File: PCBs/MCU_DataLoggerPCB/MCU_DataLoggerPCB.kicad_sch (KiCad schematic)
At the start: 25 parts, among them U1 24LC1025, U2 24LC1025, U3 DS1337S+, U4 ATMEGA328P-AU, Y1 32.768 kHz, Y2 16 MHz

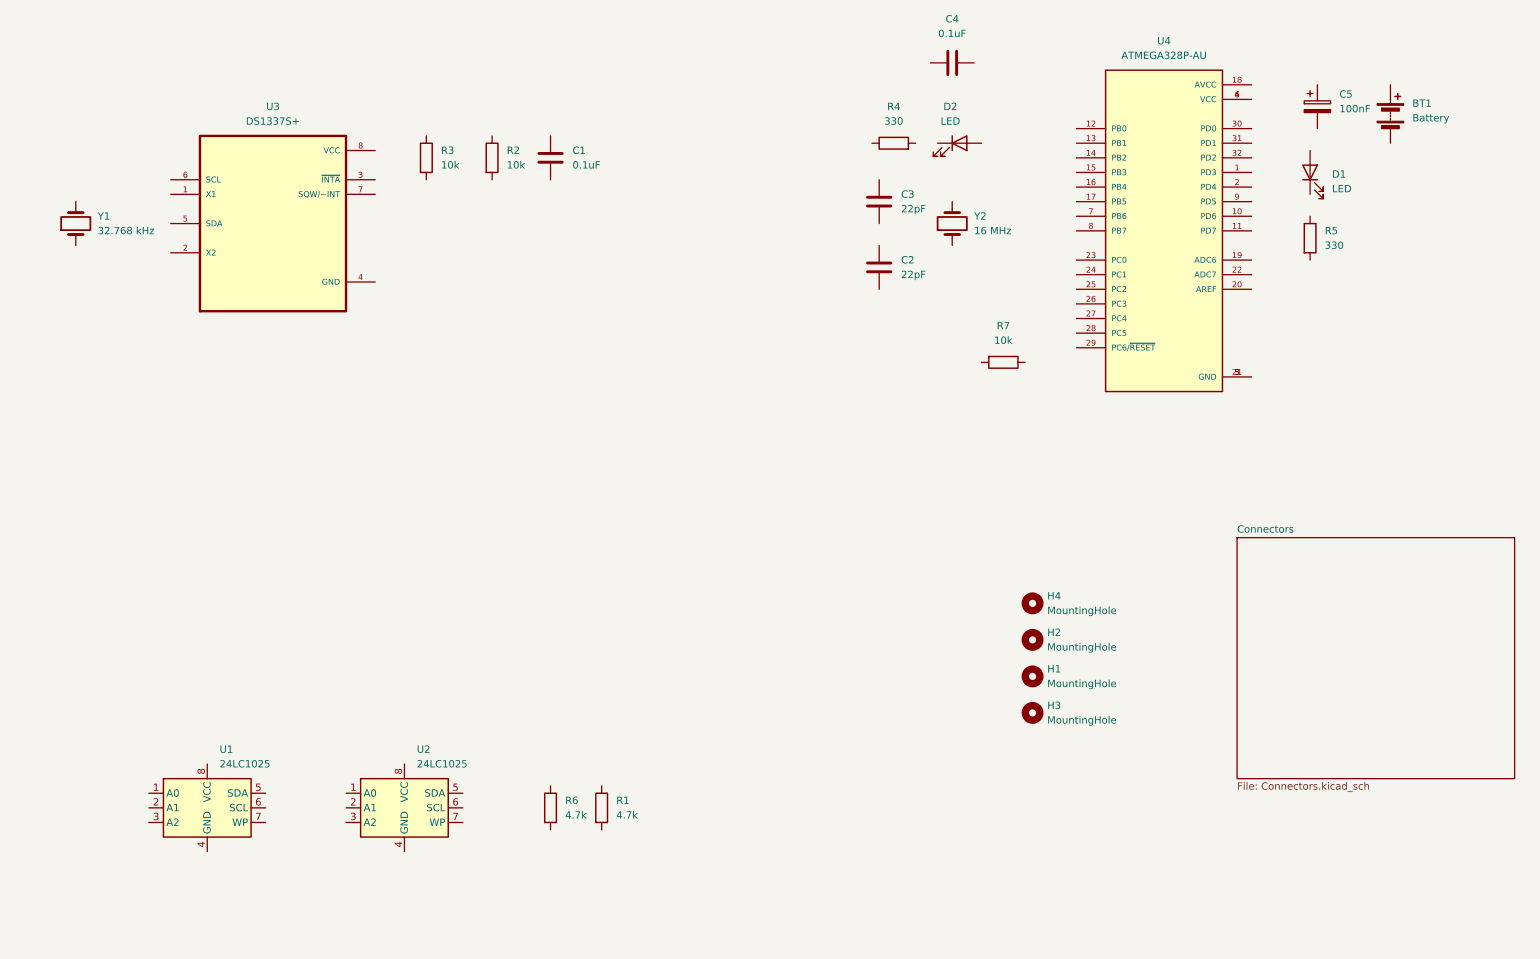
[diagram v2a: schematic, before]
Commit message: Project: completed wiring of the main sheet
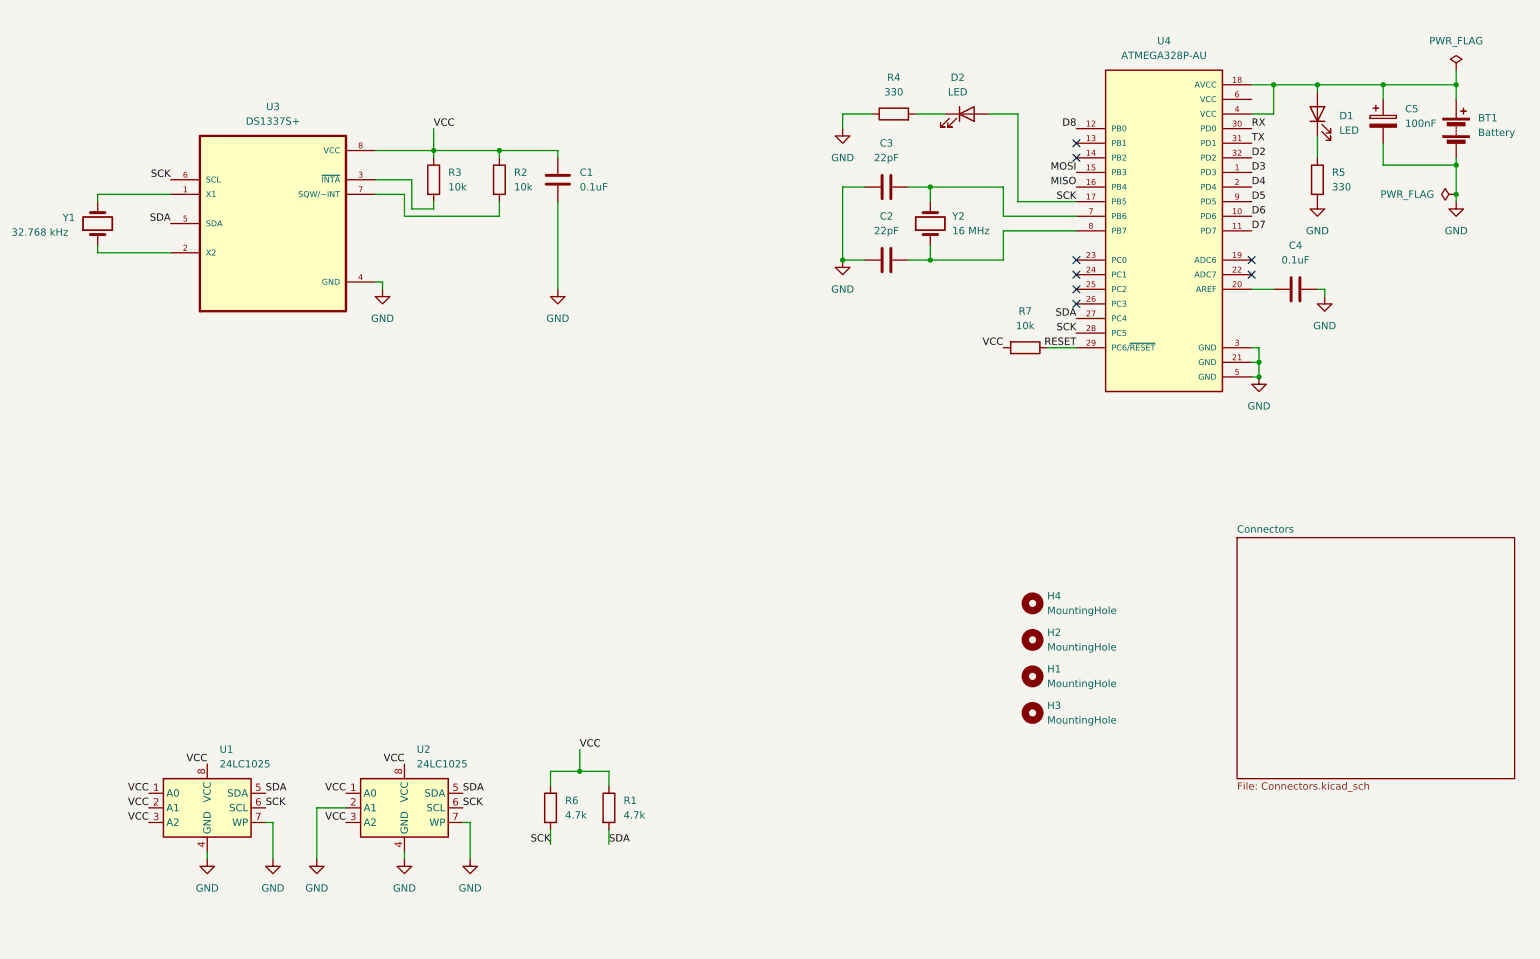
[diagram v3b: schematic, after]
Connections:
- net RESET: now reaches R7.1
- net RESET: now also U4.29 (PC6/~{RESET})
- net VCC: now reaches R7.2
- net VCC: now also C1.1, R1.1, R2.1, R3.1, R6.1, U1.1 (A0), U1.2 (A1), U1.3 (A2), U1.8 (VCC), U2.1 (A0), U2.3 (A2), U2.8 (VCC), U3.8 (VCC)
- net at R3.2: now also U3.3 (~{INTA})
- net at U3.1 (X1): now also Y1.2
- net at U3.2 (X2): now also Y1.1
- net GND: now reaches U3.4 (GND)
- net GND: now also BT1.2 (-), C1.2, C2.1, C3.1, C4.2, C5.2, R4.1, R5.2, U1.4 (GND), U1.7 (WP), U2.2 (A1), U2.4 (GND), U2.7 (WP), U4.21 (GND), U4.3 (GND), U4.5 (GND)
- net SDA: now reaches U3.5 (SDA)
- net SDA: now also R1.2, U1.5 (SDA), U2.5 (SDA), U4.27 (PC4)
- net SCK: now reaches U3.6 (SCL)
- net SCK: now also D2.2 (A), R6.2, U1.6 (SCL), U2.6 (SCL), U4.17 (PB5), U4.28 (PC5)
- net at U3.7 (SQW/~INT): now also R2.2
- net at C3.2: now also U4.7 (PB6), Y2.2
- net at C2.2: now also U4.8 (PB7), Y2.1
- net at D1.1 (K): now also R5.1
- net at D1.2 (A): now also BT1.1 (+), C5.1, U4.18 (AVCC), U4.4 (VCC)
- net D3: now reaches U4.1 (PD3)
- net D6: now reaches U4.10 (PD6)
- net D7: now reaches U4.11 (PD7)
- net D8: now reaches U4.12 (PB0)
- net MOSI: now reaches U4.15 (PB3)
- net MISO: now reaches U4.16 (PB4)
- net D4: now reaches U4.2 (PD4)
- net at U4.20 (AREF): now also C4.1
- net RX: now reaches U4.30 (PD0)
- net TX: now reaches U4.31 (PD1)
- net D2: now reaches U4.32 (PD2)
- net at U4.6 (VCC): no longer U4.4 (VCC)
- net D5: now reaches U4.9 (PD5)
- net at D2.1 (K): now also R4.2
- no-connect marks 0 -> 8
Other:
- moved on the sheet: BT1, C1, C2, C3, C4, C5, D1, D2, R1, R2, R3, R4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

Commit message: Project: completed wiring the second sheet
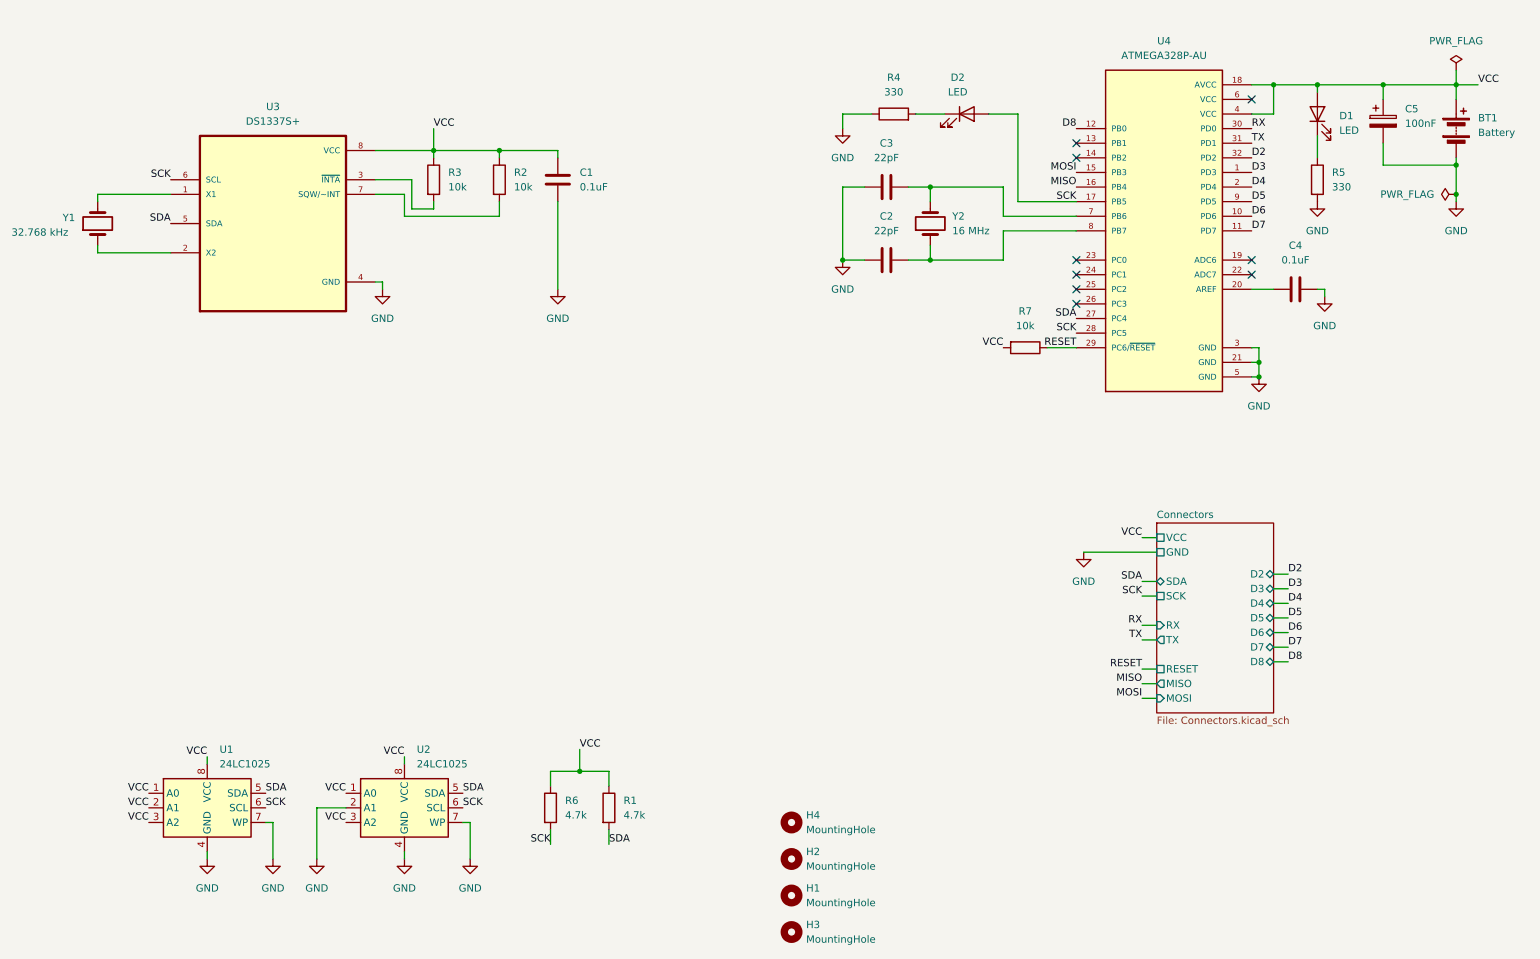
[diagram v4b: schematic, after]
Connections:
- net VCC: now also BT1.1 (+), C5.1, D1.2 (A), U4.18 (AVCC), U4.4 (VCC)
- no-connect marks 8 -> 9
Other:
- sheet Connectors ports: added D2, D3, D4, D5, D6, D7, D8, GND, MISO, MOSI, RESET, RX, SCK, SDA, TX, VCC; removed none
- moved on the sheet: H1, H2, H3, H4
